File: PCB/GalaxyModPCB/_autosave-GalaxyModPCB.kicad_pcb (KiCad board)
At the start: 2 copper layers, 63.5 x 38.2 mm, 66 parts, among them J1 LED RGBW Connector, J2 USB to UART, J3 Motor Connector, J4 Projector Connector, J5 Debug Header, J6 Power Header, J7 Boot mode, Q1 IRLML0030, Q2 IRLML0030, Q3 IRLML0030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

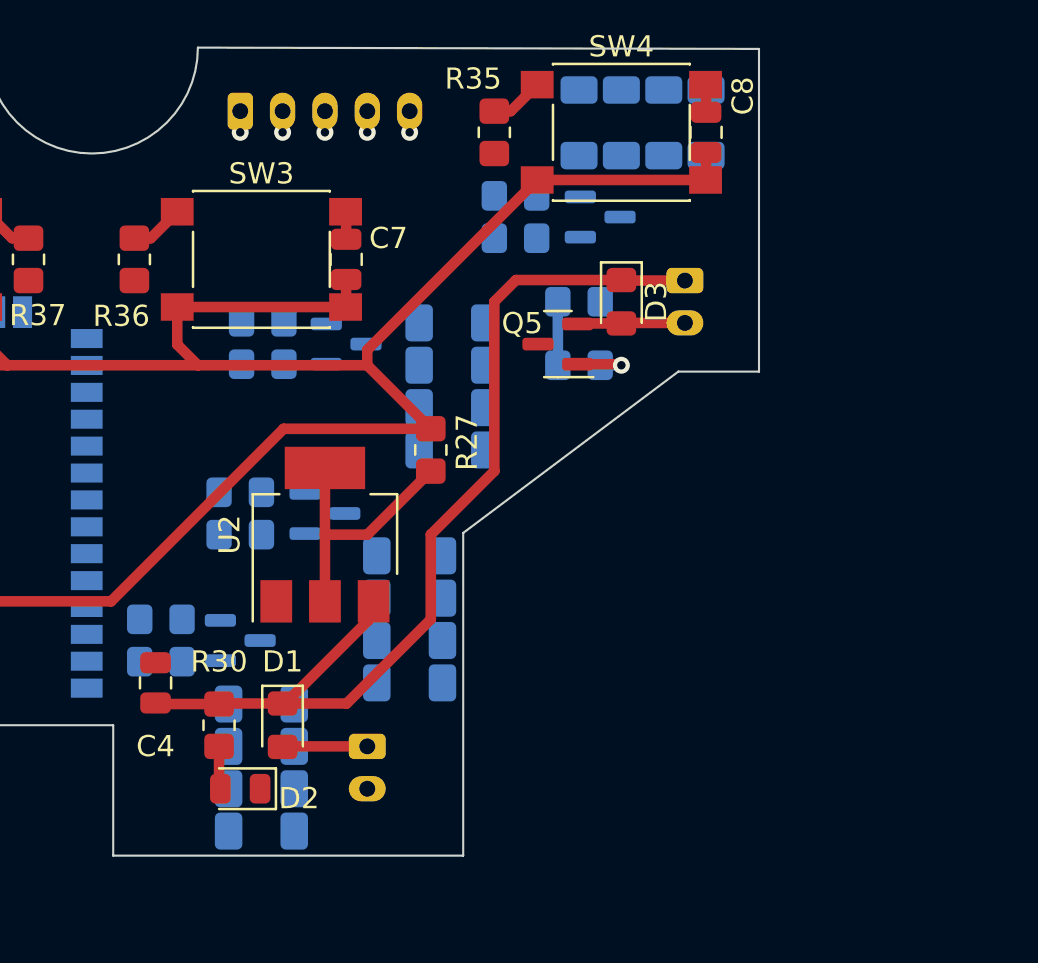
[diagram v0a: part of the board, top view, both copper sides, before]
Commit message: LED circuitry arrangement draft
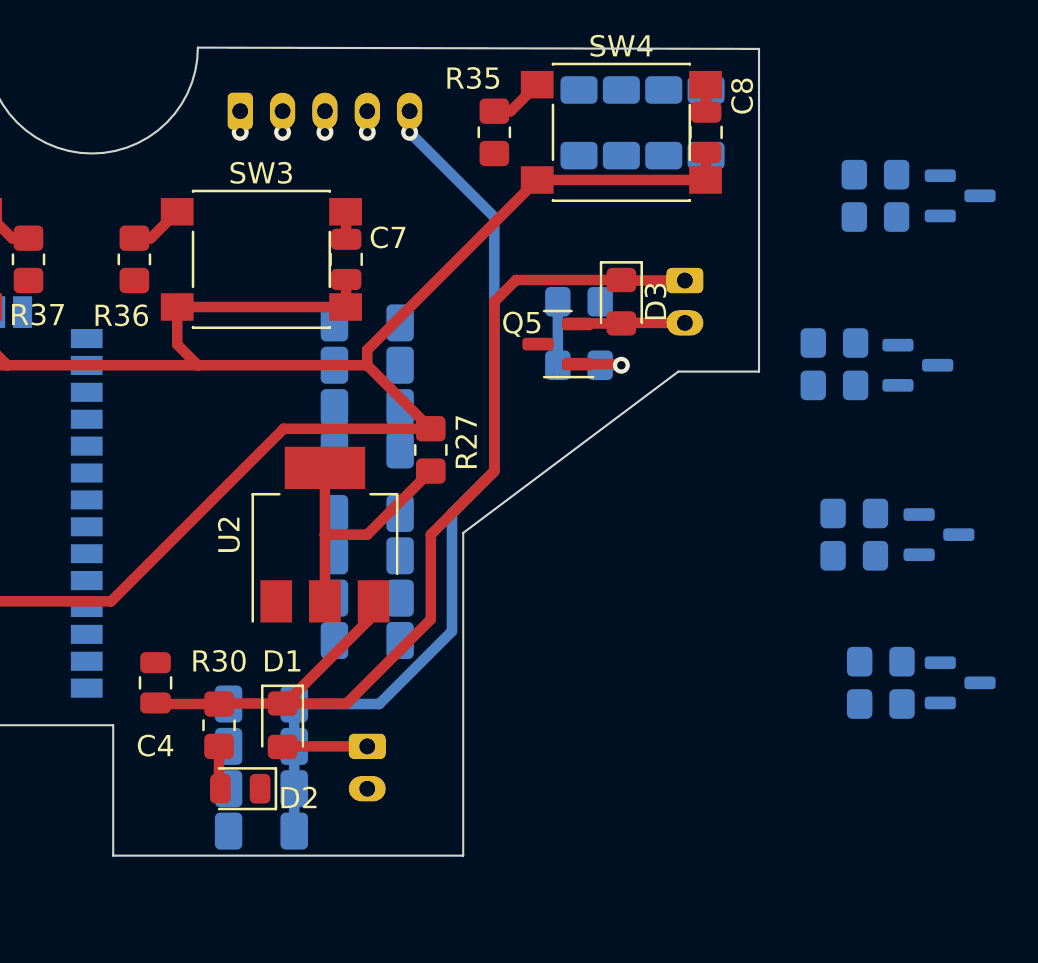
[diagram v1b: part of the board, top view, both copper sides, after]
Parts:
- moved Q4 34.1 mm to (183.0, 81.0)
- moved R20 34.1 mm to (179.3, 82.0)
- moved R24 34.1 mm to (179.3, 80.0)
- moved Q3 29.0 mm to (182.0, 74.0)
- moved R19 29.0 mm to (178.0, 75.0)
- moved R23 29.0 mm to (178.0, 73.0)
- moved Q2 27.0 mm to (181.0, 66.0)
- moved R18 27.0 mm to (177.1, 67.0)
- moved R22 27.0 mm to (177.1, 65.0)
- moved Q1 17.0 mm to (183.0, 58.0)
- moved R17 17.0 mm to (179.0, 59.0)
- moved R21 17.0 mm to (179.0, 57.0)
- moved R5 4.00 mm to (155.0, 64.0)
- moved R6 4.00 mm to (155.0, 66.0)
- moved R7 4.00 mm to (155.0, 68.0)
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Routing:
- net Net-(J1-Pad5): track 1.00 -> 41.9 mm
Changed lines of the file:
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@@
   )
   (footprint "Resistor_SMD:R_0805_2012Metric_Pad1.20x1.40mm_HandSolder" (layer "B.Cu")
-    (at 162 60)
+    (at 179 59)
     (descr "Resistor SMD 0805 (2012 Metric), square (rectangular) end terminal, IPC_7351 nominal with elongated pad for handsoldering. (Body size source: IPC-SM-782 page 72, https://www.pcb-3d.com/wordpress/wp-content/uploads/ipc-sm-782a_amendment_1_and_2.pdf), generated with kicad-footprint-generator")
     (tags "resistor handsolder")
@@
   )
   (footprint "Resistor_SMD:R_1206_3216Metric_Pad1.30x1.75mm_HandSolder" (layer "B.Cu")
-    (at 157 81 180)
+    (at 155 79 180)
     (descr "Resistor SMD 1206 (3216 Metric), square (rectangular) end terminal, IPC_7351 nominal with elongated pad for handsoldering. (Body size source: IPC-SM-782 page 72, https://www.pcb-3d.com/wordpress/wp-content/uploads/ipc-sm-782a_amendment_1_and_2.pdf), generated with kicad-footprint-generator")
     (tags "resistor handsolder")
@@
   )
   (footprint "Package_TO_SOT_SMD:SOT-23" (layer "B.Cu")
-    (at 166 59)
+    (at 183 58)
     (descr "SOT, 3 Pin (https://www.jedec.org/system/files/docs/to-236h.pdf variant AB), generated with kicad-footprint-generator ipc_gullwing_generator.py")
     (tags "SOT TO_SOT_SMD")
@@
   )
   (footprint "Resistor_SMD:R_0805_2012Metric_Pad1.20x1.40mm_HandSolder" (layer "B.Cu")
-    (at 149 74)
+    (at 178 75)
     (descr "Resistor SMD 0805 (2012 Metric), square (rectangular) end terminal, IPC_7351 nominal with elongated pad for handsoldering. (Body size source: IPC-SM-782 page 72, https://www.pcb-3d.com/wordpress/wp-content/uploads/ipc-sm-782a_amendment_1_and_2.pdf), generated with kicad-footprint-generator")
     (tags "resistor handsolder")
@@
   )
   (footprint "Package_TO_SOT_SMD:SOT-23" (layer "B.Cu")
-    (at 153 73)
+    (at 182 74)
     (descr "SOT, 3 Pin (https://www.jedec.org/system/files/docs/to-236h.pdf variant AB), generated with kicad-footprint-generator ipc_gullwing_generator.py")
     (tags "SOT TO_SOT_SMD")
@@
   )
   (footprint "Package_TO_SOT_SMD:SOT-23" (layer "B.Cu")
-    (at 154 65)
+    (at 181 66)
     (descr "SOT, 3 Pin (https://www.jedec.org/system/files/docs/to-236h.pdf variant AB), generated with kicad-footprint-generator ipc_gullwing_generator.py")
     (tags "SOT TO_SOT_SMD")
@@
   )
   (footprint "Resistor_SMD:R_1206_3216Metric_Pad1.30x1.75mm_HandSolder" (layer "B.Cu")
-    (at 157 77 180)
+    (at 155 75 180)
     (descr "Resistor SMD 1206 (3216 Metric), square (rectangular) end terminal, IPC_7351 nominal with elongated pad for handsoldering. (Body size source: IPC-SM-782 page 72, https://www.pcb-3d.com/wordpress/wp-content/uploads/ipc-sm-782a_amendment_1_and_2.pdf), generated with kicad-footprint-generator")
     (tags "resistor handsolder")
@@
   )
   (footprint "Resistor_SMD:R_1206_3216Metric_Pad1.30x1.75mm_HandSolder" (layer "B.Cu")
-    (at 157 79 180)
+    (at 155 77 180)
     (descr "Resistor SMD 1206 (3216 Metric), square (rectangular) end terminal, IPC_7351 nominal with elongated pad for handsoldering. (Body size source: IPC-SM-782 page 72, https://www.pcb-3d.com/wordpress/wp-content/uploads/ipc-sm-782a_amendment_1_and_2.pdf), generated with kicad-footprint-generator")
     (tags "resistor handsolder")
@@
   )
   (footprint "Resistor_SMD:R_1206_3216Metric_Pad1.30x1.75mm_HandSolder" (layer "B.Cu")
-    (at 159 64 180)
+    (at 155 64 180)
     (descr "Resistor SMD 1206 (3216 Metric), square (rectangular) end terminal, IPC_7351 nominal with elongated pad for handsoldering. (Body size source: IPC-SM-782 page 72, https://www.pcb-3d.com/wordpress/wp-content/uploads/ipc-sm-782a_amendment_1_and_2.pdf), generated with kicad-footprint-generator")
     (tags "resistor handsolder")
@@
   )
   (footprint "Resistor_SMD:R_0805_2012Metric_Pad1.20x1.40mm_HandSolder" (layer "B.Cu")
-    (at 149 72 180)
+    (at 178 73 180)
     (descr "Resistor SMD 0805 (2012 Metric), square (rectangular) end terminal, IPC_7351 nominal with elongated pad for handsoldering. (Body size source: IPC-SM-782 page 72, https://www.pcb-3d.com/wordpress/wp-content/uploads/ipc-sm-782a_amendment_1_and_2.pdf), generated with kicad-footprint-generator")
     (tags "resistor handsolder")
@@
   )
   (footprint "Resistor_SMD:R_1206_3216Metric_Pad1.30x1.75mm_HandSolder" (layer "B.Cu")
-    (at 159 68 180)
+    (at 155 68 180)
     (descr "Resistor SMD 1206 (3216 Metric), square (rectangular) end terminal, IPC_7351 nominal with elongated pad for handsoldering. (Body size source: IPC-SM-782 page 72, https://www.pcb-3d.com/wordpress/wp-content/uploads/ipc-sm-782a_amendment_1_and_2.pdf), generated with kicad-footprint-generator")
     (tags "resistor handsolder")
@@
   )
   (footprint "Resistor_SMD:R_0805_2012Metric_Pad1.20x1.40mm_HandSolder" (layer "B.Cu")
-    (at 150.0625 63.95 180)
+    (at 177.0625 64.95 180)
     (descr "Resistor SMD 0805 (2012 Metric), square (rectangular) end terminal, IPC_7351 nominal with elongated pad for handsoldering. (Body size source: IPC-SM-782 page 72, https://www.pcb-3d.com/wordpress/wp-content/uploads/ipc-sm-782a_amendment_1_and_2.pdf), generated with kicad-footprint-generator")
     (tags "resistor handsolder")
@@
   )
   (footprint "Resistor_SMD:R_0805_2012Metric_Pad1.20x1.40mm_HandSolder" (layer "B.Cu")
-    (at 145.253928 80)
+    (at 179.253928 82)
     (descr "Resistor SMD 0805 (2012 Metric), square (rectangular) end terminal, IPC_7351 nominal with elongated pad for handsoldering. (Body size source: IPC-SM-782 page 72, https://www.pcb-3d.com/wordpress/wp-content/uploads/ipc-sm-782a_amendment_1_and_2.pdf), generated with kicad-footprint-generator")
     (tags "resistor handsolder")
@@
   )
   (footprint "Package_TO_SOT_SMD:SOT-23" (layer "B.Cu")
-    (at 149 79)
+    (at 183 81)
     (descr "SOT, 3 Pin (https://www.jedec.org/system/files/docs/to-236h.pdf variant AB), generated with kicad-footprint-generator ipc_gullwing_generator.py")
     (tags "SOT TO_SOT_SMD")
@@
   )
   (footprint "Resistor_SMD:R_0805_2012Metric_Pad1.20x1.40mm_HandSolder" (layer "B.Cu")
-    (at 150.0625 65.95)
+    (at 177.0625 66.95)
     (descr "Resistor SMD 0805 (2012 Metric), square (rectangular) end terminal, IPC_7351 nominal with elongated pad for handsoldering. (Body size source: IPC-SM-782 page 72, https://www.pcb-3d.com/wordpress/wp-content/uploads/ipc-sm-782a_amendment_1_and_2.pdf), generated with kicad-footprint-generator")
     (tags "resistor handsolder")
@@
   )
   (footprint "Resistor_SMD:R_1206_3216Metric_Pad1.30x1.75mm_HandSolder" (layer "B.Cu")
-    (at 159 70 180)
+    (at 155 70 180)
     (descr "Resistor SMD 1206 (3216 Metric), square (rectangular) end terminal, IPC_7351 nominal with elongated pad for handsoldering. (Body size source: IPC-SM-782 page 72, https://www.pcb-3d.com/wordpress/wp-content/uploads/ipc-sm-782a_amendment_1_and_2.pdf), generated with kicad-footprint-generator")
     (tags "resistor handsolder")
@@
   )
   (footprint "Resistor_SMD:R_1206_3216Metric_Pad1.30x1.75mm_HandSolder" (layer "B.Cu")
-    (at 159 66 180)
+    (at 155 66 180)
     (descr "Resistor SMD 1206 (3216 Metric), square (rectangular) end terminal, IPC_7351 nominal with elongated pad for handsoldering. (Body size source: IPC-SM-782 page 72, https://www.pcb-3d.com/wordpress/wp-content/uploads/ipc-sm-782a_amendment_1_and_2.pdf), generated with kicad-footprint-generator")
     (tags "resistor handsolder")
@@
   )
   (footprint "Resistor_SMD:R_0805_2012Metric_Pad1.20x1.40mm_HandSolder" (layer "B.Cu")
-    (at 145.253928 78 180)
+    (at 179.253928 80 180)
     (descr "Resistor SMD 0805 (2012 Metric), square (rectangular) end terminal, IPC_7351 nominal with elongated pad for handsoldering. (Body size source: IPC-SM-782 page 72, https://www.pcb-3d.com/wordpress/wp-content/uploads/ipc-sm-782a_amendment_1_and_2.pdf), generated with kicad-footprint-generator")
     (tags "resistor handsolder")
@@
   )
   (footprint "Resistor_SMD:R_0805_2012Metric_Pad1.20x1.40mm_HandSolder" (layer "B.Cu")
-    (at 162 58 180)
+    (at 179 57 180)
     (descr "Resistor SMD 0805 (2012 Metric), square (rectangular) end terminal, IPC_7351 nominal with elongated pad for handsoldering. (Body size source: IPC-SM-782 page 72, https://www.pcb-3d.com/wordpress/wp-content/uploads/ipc-sm-782a_amendment_1_and_2.pdf), generated with kicad-footprint-generator")
     (tags "resistor handsolder")
@@
   )
   (footprint "Resistor_SMD:R_1206_3216Metric_Pad1.30x1.75mm_HandSolder" (layer "B.Cu")
-    (at 157 75 180)
+    (at 155 73 180)
     (descr "Resistor SMD 1206 (3216 Metric), square (rectangular) end terminal, IPC_7351 nominal with elongated pad for handsoldering. (Body size source: IPC-SM-782 page 72, https://www.pcb-3d.com/wordpress/wp-content/uploads/ipc-sm-782a_amendment_1_and_2.pdf), generated with kicad-footprint-generator")
     (tags "resistor handsolder")
@@
   (segment (start 157 54) (end 157 55) (width 0.5) (layer "F.Cu") (net 12))
   (via (at 157 55) (size 0.8) (drill 0.4) (layers "F.Cu" "B.Cu") (net 12))
+  (segment (start 159 78.564949) (end 159 73) (width 0.5) (layer "B.Cu") (net 12))
+  (segment (start 159 73) (end 161 71) (width 0.5) (layer "B.Cu") (net 12))
+  (segment (start 151.55 86) (end 151.55 84) (width 0.5) (layer "B.Cu") (net 12))
+  (segment (start 161 71) (end 161 59) (width 0.5) (layer "B.Cu") (net 12))
+  (segment (start 161 59) (end 157 55) (width 0.5) (layer "B.Cu") (net 12))
+  (segment (start 155.564949 82) (end 159 78.564949) (width 0.5) (layer "B.Cu") (net 12))
+  (segment (start 151.55 88) (end 151.55 86) (width 0.5) (layer "B.Cu") (net 12))
+  (segment (start 151.55 82) (end 155.564949 82) (width 0.5) (layer "B.Cu") (net 12))
+  (segment (start 151.55 84) (end 151.55 82) (width 0.5) (layer "B.Cu") (net 12))
   (segment (start 113 67) (end 113 65) (width 0.5) (layer "F.Cu") (net 15))
   (segment (start 116 58) (end 116 61) (width 0.5) (layer "B.Cu") (net 16))
